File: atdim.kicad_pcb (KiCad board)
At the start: 2 copper layers, 49.8 x 24.9 mm, 17 parts, among them IC1 ATTINY85-T, P1 CONN_4, P2 ICSP, Q1 MOSFET_N, U1 7805

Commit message: switch to 47K sense resistor for better match for 5549 response
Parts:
- R1: value 10K -> 47K
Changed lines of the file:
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@@
       (effects (font (size 1.397 1.27) (thickness 0.2032)))
     )
-    (fp_text value 10K (at 0 0.127 180) (layer F.SilkS)
+    (fp_text value 47K (at 0 0.127 180) (layer F.SilkS)
       (effects (font (size 1.397 1.27) (thickness 0.2032)))
     )

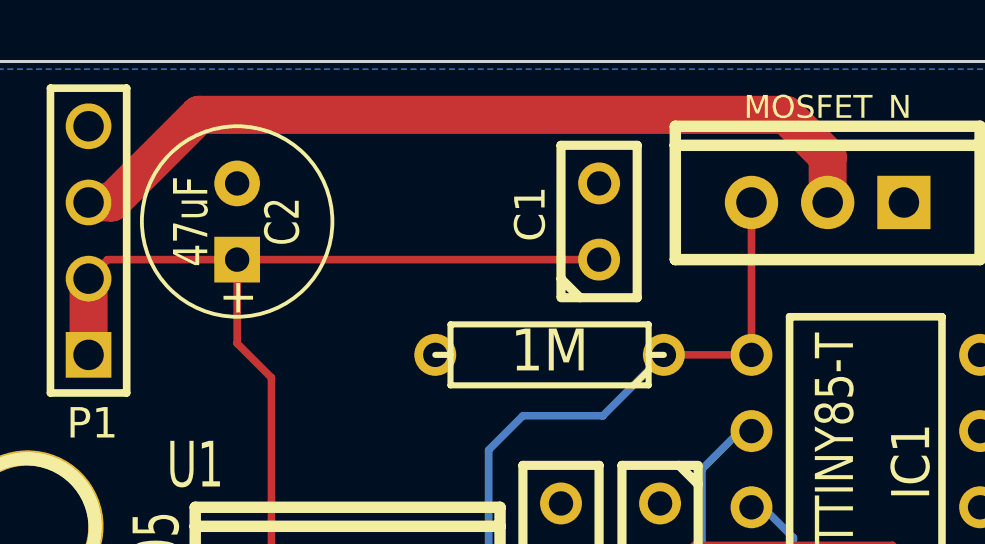
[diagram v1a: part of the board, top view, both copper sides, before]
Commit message: added pull-up resistor, changed some component values
Added pull-up resistor based on writeup at
https://gasstationwithoutpumps.wordpress.com/2014/07/28/pwm-controller/

Modified suggested capacitor values based on additional perusal of
data sheets for various versions of components.

Modified suggested R1 value based on experiments with my existing LDRs
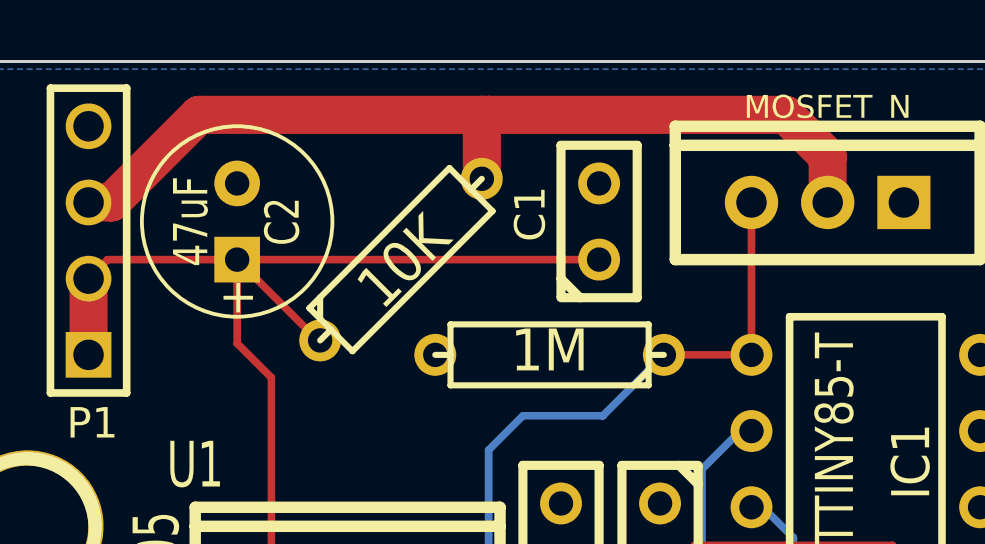
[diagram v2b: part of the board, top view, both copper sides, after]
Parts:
- added R3: 10K, R3, F.Cu at (116.3, 106.7)
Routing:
- net +12V: track 31.1 -> 35.0 mm
- net /DRAIN: track 28.0 -> 30.5 mm
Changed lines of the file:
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@@
 (kicad_pcb (version 3) (host pcbnew "(2013-june-11)-stable")
   (general
-    (links 33)
+    (links 35)
     (no_connects 0)
     (area 99.6315 100.025999 150.241 125.1966)
     (thickness 1.6)
     (drawings 4)
-    (tracks 79)
+    (tracks 86)
     (zones 0)
-    (modules 17)
+    (modules 18)
     (nets 11)
   )
@@
     )
   )
+  (module R3 (layer F.Cu)
+    (at 116.332 106.68 45)
+    (descr "Resitance 3 pas")
+    (tags R)
+    (autoplace_cost180 10)
+    (fp_text reference R3 (at 0 0.127 45) (layer F.SilkS) hide
+      (effects (font (size 1.397 1.27) (thickness 0.2032)))
+    )
+    (fp_text value 10K (at 0 0.127 45) (layer F.SilkS)
+      (effects (font (size 1.397 1.27) (thickness 0.2032)))
+    )
+    (fp_line (start -3.81 0) (end -3.302 0) (layer F.SilkS) (width 0.2032))
+    (fp_line (start 3.81 0) (end 3.302 0) (layer F.SilkS) (width 0.2032))
+    (fp_line (start 3.302 0) (end 3.302 -1.016) (layer F.SilkS) (width 0.2032))
+    (fp_line (start 3.302 -1.016) (end -3.302 -1.016) (layer F.SilkS) (width 0.2032))
+    (fp_line (start -3.302 -1.016) (end -3.302 1.016) (layer F.SilkS) (width 0.2032))
+    (fp_line (start -3.302 1.016) (end 3.302 1.016) (layer F.SilkS) (width 0.2032))
+    (fp_line (start 3.302 1.016) (end 3.302 0) (layer F.SilkS) (width 0.2032))
+    (fp_line (start -3.302 -0.508) (end -2.794 -1.016) (layer F.SilkS) (width 0.2032))
+    (pad 1 thru_hole circle (at -3.81 0 45) (size 1.397 1.397) (drill 0.8128)
+      (layers *.Cu *.Mask F.SilkS)
+      (net 1 +12V)
+    )
+    (pad 2 thru_hole circle (at 3.81 0 45) (size 1.397 1.397) (drill 0.8128)
+      (layers *.Cu *.Mask F.SilkS)
+      (net 4 /DRAIN)
+    )
+    (model discret/resistor.wrl
+      (at (xyz 0 0 0))
+      (scale (xyz 0.3 0.3 0.3))
+      (rotate (xyz 0 0 0))
+    )
+  )
   (gr_line (start 100.076 124.968) (end 100.076 100.076) (angle 90) (layer Edge.Cuts) (width 0.1))
   (gr_line (start 149.86 124.968) (end 100.076 124.968) (angle 90) (layer Edge.Cuts) (width 0.1))
   (gr_line (start 149.86 100.076) (end 149.86 124.968) (angle 90) (layer Edge.Cuts) (width 0.1))
   (gr_line (start 100.076 100.076) (end 149.86 100.076) (angle 90) (layer Edge.Cuts) (width 0.1))
+  (segment (start 113.637923 109.374077) (end 113.565077 109.374077) (width 0.254) (layer F.Cu) (net 1))
+  (segment (start 113.565077 109.374077) (end 110.871 106.68) (width 0.254) (layer F.Cu) (net 1))
   (segment (start 110.871 106.68) (end 110.871 109.474) (width 0.254) (layer F.Cu) (net 1))
   (segment (start 112.014 110.617) (end 112.014 117.475) (width 0.254) (layer F.Cu) (net 1))
@@
   (segment (start 137.16 115.697) (end 137.16 121.793) (width 0.254) (layer F.Cu) (net 3))
   (segment (start 136.398 114.935) (end 137.16 115.697) (width 0.254) (layer F.Cu) (net 3))
+  (segment (start 119.026077 103.985923) (end 119.026077 101.854) (width 1.27) (layer F.Cu) (net 4))
+  (segment (start 119.253 101.981) (end 119.253 101.854) (width 1.27) (layer F.Cu) (net 4))
+  (segment (start 119.153077 101.981) (end 119.253 101.981) (width 1.27) (layer F.Cu) (net 4))
+  (segment (start 119.026077 101.854) (end 119.153077 101.981) (width 1.27) (layer F.Cu) (net 4))
   (segment (start 105.918 104.775) (end 106.68 104.775) (width 1.27) (layer F.Cu) (net 4))
   (segment (start 130.556 103.251) (end 130.556 104.775) (width 1.27) (layer F.Cu) (net 4))
   (segment (start 129.159 101.854) (end 130.556 103.251) (width 1.27) (layer F.Cu) (net 4))
-  (segment (start 109.601 101.854) (end 129.159 101.854) (width 1.27) (layer F.Cu) (net 4))
+  (segment (start 109.601 101.854) (end 119.253 101.854) (width 1.27) (layer F.Cu) (net 4))
+  (segment (start 119.253 101.854) (end 129.159 101.854) (width 1.27) (layer F.Cu) (net 4))
   (segment (start 106.68 104.775) (end 109.601 101.854) (width 1.27) (layer F.Cu) (net 4))
   (segment (start 113.538 121.92) (end 114.935 123.317) (width 0.254) (layer B.Cu) (net 5))

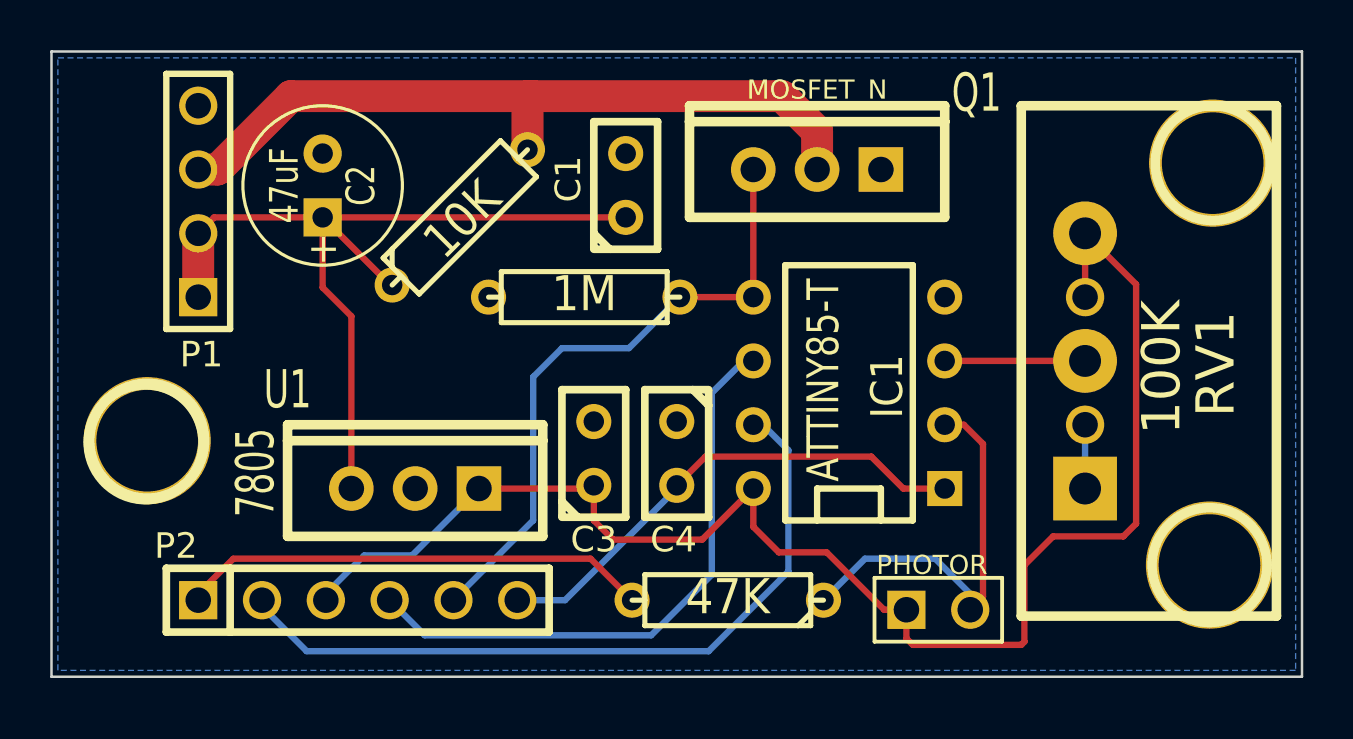
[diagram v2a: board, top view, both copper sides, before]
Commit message: add annotations on silkscreen for parts and connections
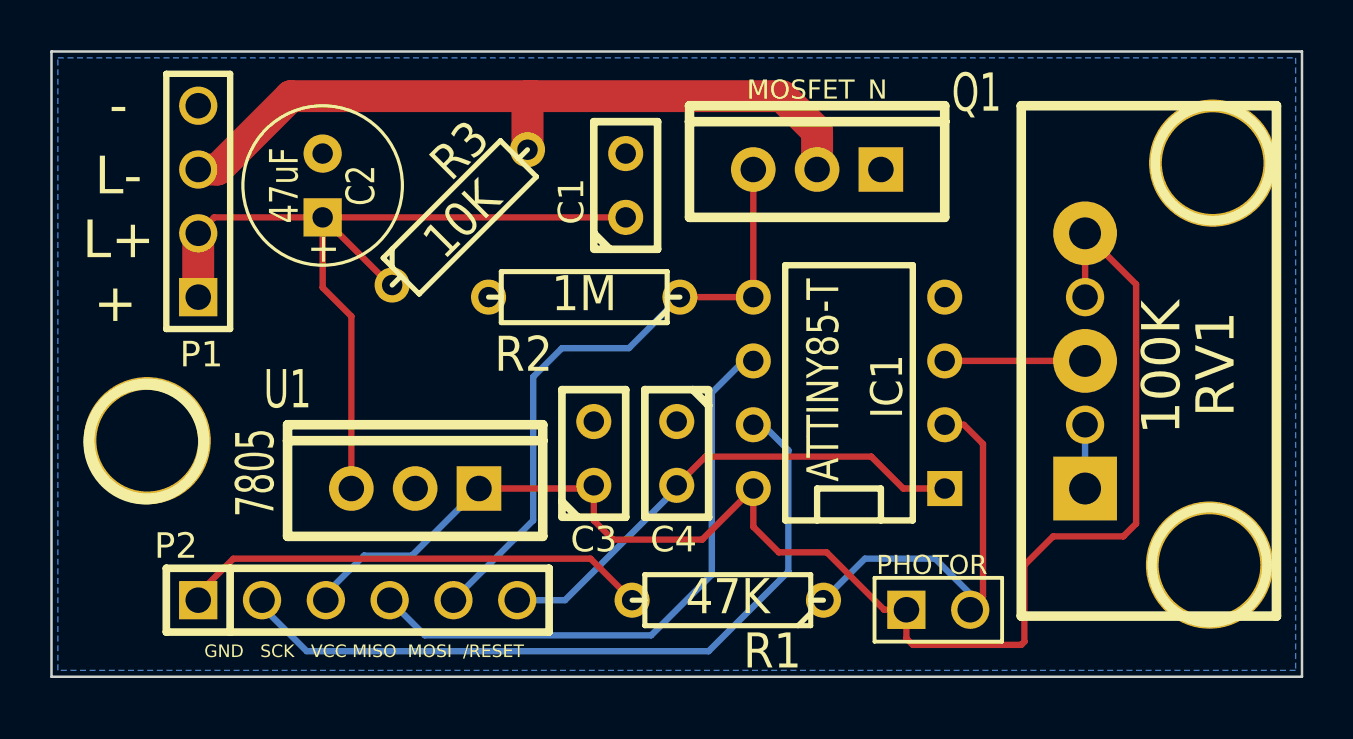
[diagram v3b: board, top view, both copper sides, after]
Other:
- board text added: "+"
- board text added: "-"
- board text added: "GND SCK VCC MISO MOSI /RESET"
- board text added: "L+"
- board text added: "L-"
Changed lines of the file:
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@@
     (links 35)
     (no_connects 0)
-    (area 99.6315 100.025999 150.241 125.1966)
+    (area 99.6315 100.025999 150.241 125.2601)
     (thickness 1.6)
-    (drawings 4)
+    (drawings 9)
     (tracks 86)
     (zones 0)
@@
     (tags R)
     (autoplace_cost180 10)
-    (fp_text reference R2 (at 0 0.127 180) (layer F.SilkS) hide
+    (fp_text reference R2 (at 2.413 -2.286 180) (layer F.SilkS)
       (effects (font (size 1.397 1.27) (thickness 0.2032)))
     )
@@
     (tags R)
     (autoplace_cost180 10)
-    (fp_text reference R1 (at 0 0.127 180) (layer F.SilkS) hide
+    (fp_text reference R1 (at -1.778 -2.032 180) (layer F.SilkS)
       (effects (font (size 1.397 1.27) (thickness 0.2032)))
     )
@@
     (descr "Condensateur e = 1 pas")
     (tags C)
-    (fp_text reference C1 (at 0.254 -2.286 90) (layer F.SilkS)
+    (fp_text reference C1 (at -0.635 -2.159 90) (layer F.SilkS)
       (effects (font (size 1.016 1.016) (thickness 0.2032)))
     )
@@
     (tags R)
     (autoplace_cost180 10)
-    (fp_text reference R3 (at 0 0.127 45) (layer F.SilkS) hide
+    (fp_text reference R3 (at 1.885854 -1.885854 45) (layer F.SilkS)
       (effects (font (size 1.397 1.27) (thickness 0.2032)))
     )
@@
     )
   )
+  (gr_text "GND   SCK   VCC MISO  MOSI  /RESET" (at 112.522 123.952) (layer F.SilkS)
+    (effects (font (size 0.5 0.5) (thickness 0.125)))
+  )
+  (gr_text L- (at 102.743 105.029) (layer F.SilkS)
+    (effects (font (size 1.5 1.5) (thickness 0.3)))
+  )
+  (gr_text L+ (at 102.743 107.569) (layer F.SilkS)
+    (effects (font (size 1.5 1.5) (thickness 0.3)))
+  )
+  (gr_text + (at 102.616 110.109) (layer F.SilkS)
+    (effects (font (size 1.5 1.5) (thickness 0.3)))
+  )
+  (gr_text - (at 102.743 102.235) (layer F.SilkS)
+    (effects (font (size 1.5 1.5) (thickness 0.3)))
+  )
   (gr_line (start 100.076 124.968) (end 100.076 100.076) (angle 90) (layer Edge.Cuts) (width 0.1))

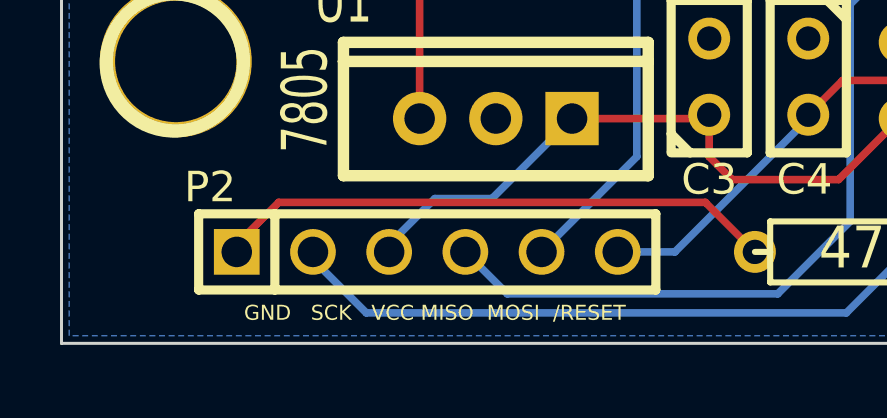
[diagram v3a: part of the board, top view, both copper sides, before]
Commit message: mark RESET pin with overbar
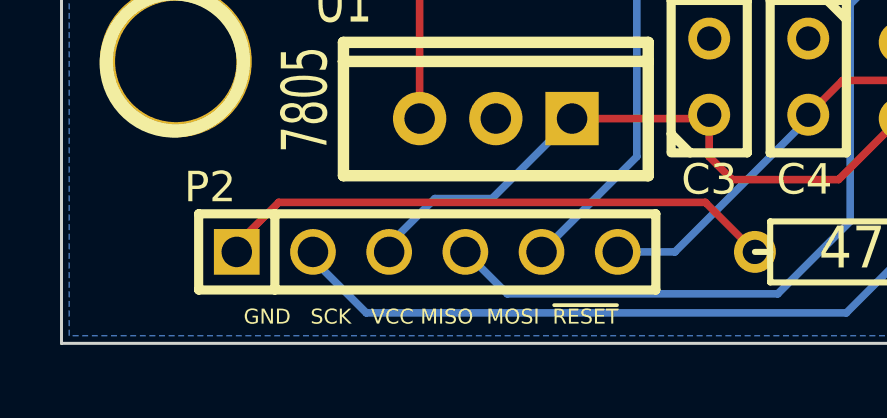
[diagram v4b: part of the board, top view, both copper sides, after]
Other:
- board text added: "GND SCK VCC MISO MOSI ~RESET"
- board text removed: "GND SCK VCC MISO MOSI /RESET"
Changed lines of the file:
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@@
     )
   )
-  (gr_text "GND   SCK   VCC MISO  MOSI  /RESET" (at 112.522 123.952) (layer F.SilkS)
+  (gr_text "GND   SCK   VCC MISO  MOSI  ~RESET" (at 112.395 124.079) (layer F.SilkS)
     (effects (font (size 0.5 0.5) (thickness 0.125)))
   )

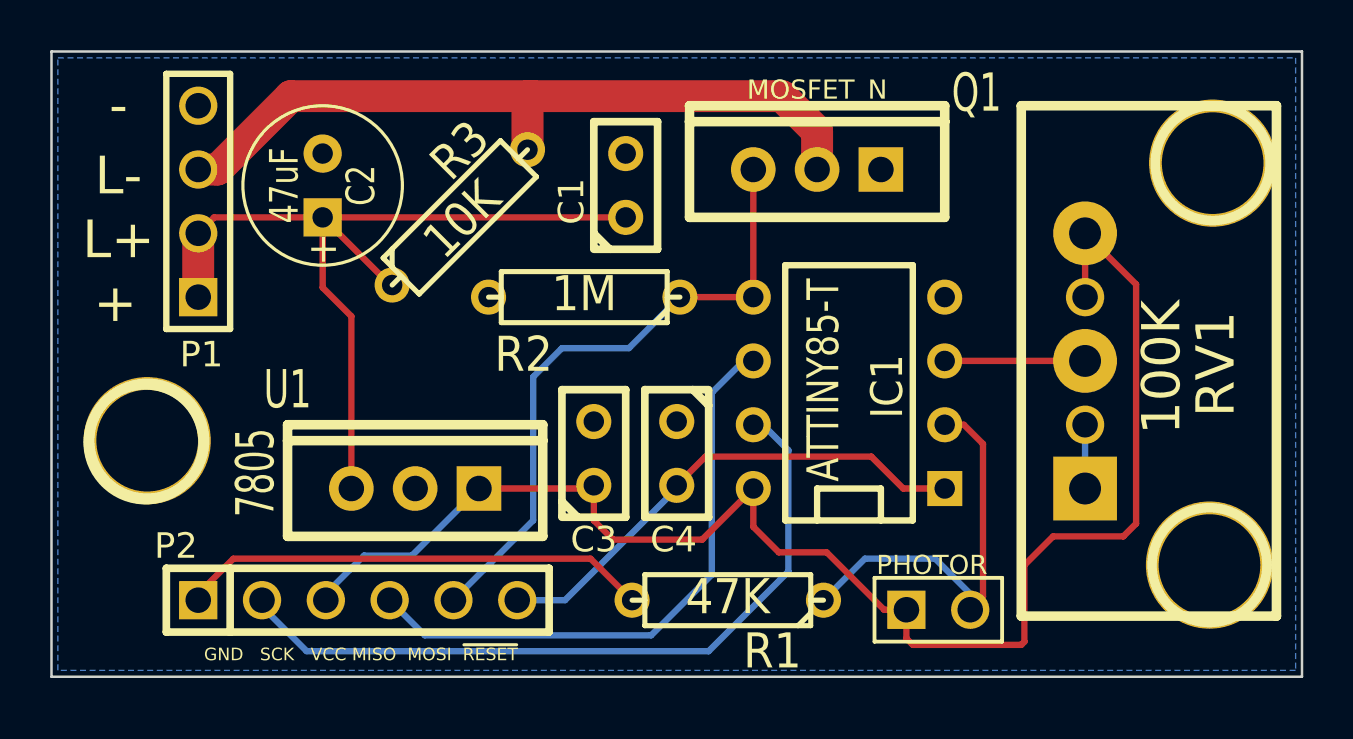
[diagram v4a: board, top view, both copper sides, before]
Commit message: rearrange board: separate power from logic, no need for reverse mounting or folding capacitor leads
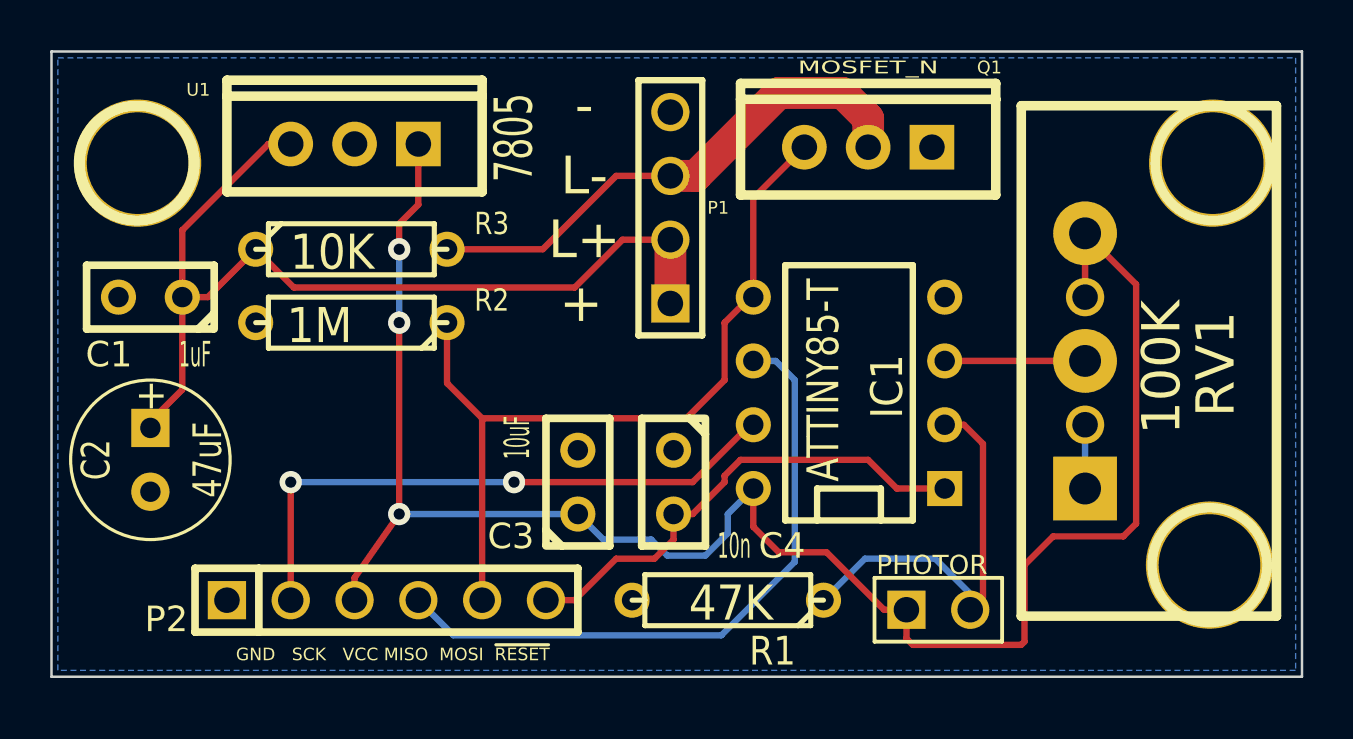
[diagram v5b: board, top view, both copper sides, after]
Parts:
- removed the 1PIN at (103.9, 115.6)
- removed the 1PIN at (103.8, 115.6)
- added 1PIN: P***, 1pin, F.Cu at (103.5, 104.5)
- added 1PIN: P***, 1pin, F.Cu at (103.4, 104.5)
- moved C1 19.4 mm to (104.0, 109.9), turned to 180 degrees
- moved P1 18.8 mm to (124.7, 106.3)
- moved U1 13.9 mm to (112.1, 103.8)
- moved C2 12.9 mm to (104.0, 116.3), turned to 270 degrees
- moved R2 9.33 mm to (112.0, 110.9)
- moved R3 4.50 mm to (112.0, 108.0), turned to 0 degrees
- moved Q1 2.22 mm to (132.6, 103.9)
- moved C3 1.31 mm to (121.0, 117.2)
- moved C4 1.15 mm to (124.8, 117.2)
- moved P2 1.14 mm to (113.4, 121.9)
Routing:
- net GND: track 21.3 -> 2.54 mm
- net /VCC: track 59.7 -> 73.5 mm, vias 0 -> 3
- net /DRAIN: track 30.5 -> 20.9 mm
- net /MOSI: track 25.4 -> 32.6 mm
- net +12V: track 35.0 -> 40.9 mm
- net /SCK: track 29.9 -> 24.1 mm, vias 0 -> 2
- net /MISO: track 23.8 -> 26.0 mm
- net /~RESET: track 20.0 -> 19.4 mm

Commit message: add a fusible resistor
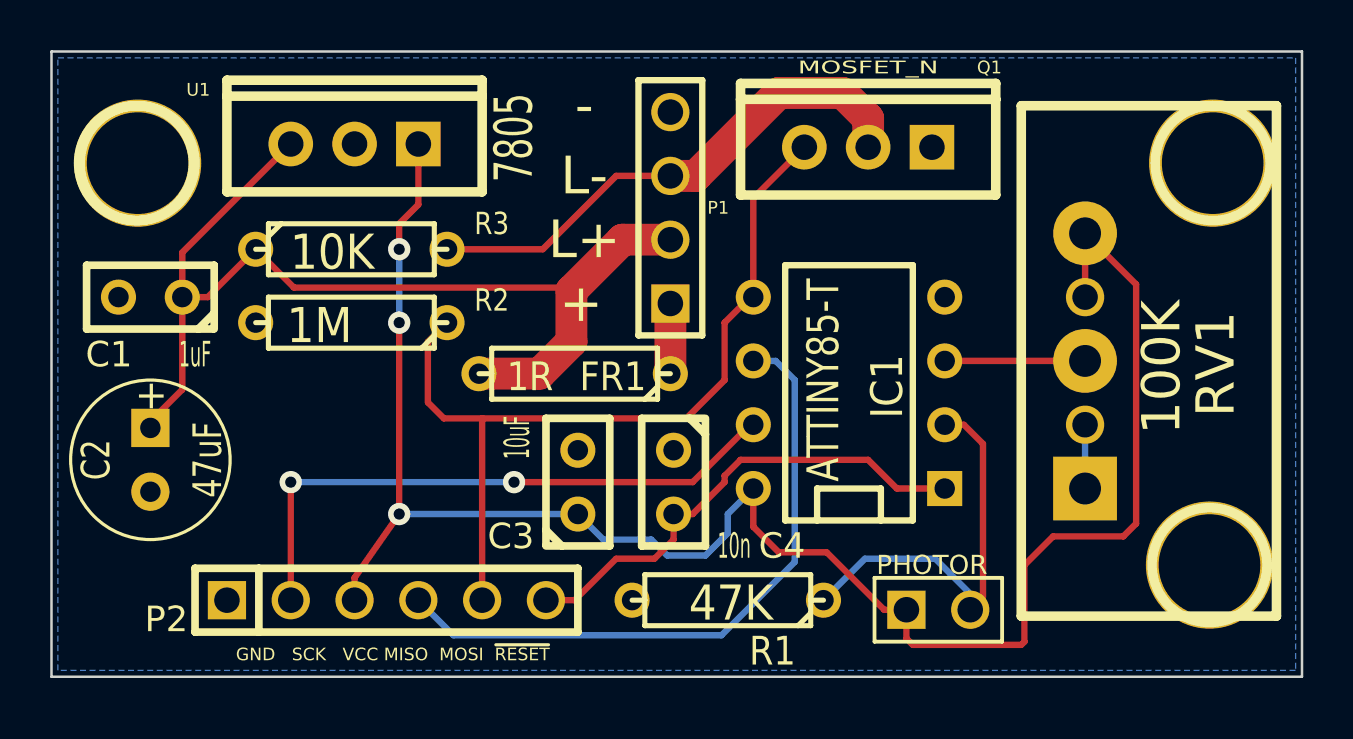
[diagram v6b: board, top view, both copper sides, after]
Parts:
- added FR1: 1R, R3, F.Cu at (120.9, 112.9)
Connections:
- C1 pad 1: +12V -> /+12VS
- C2 pad 1: +12V -> /+12VS
- P1 pad 2: +12V -> /+12VS
- R3 pad 1: +12V -> /+12VS
- U1 pad VI: +12V -> /+12VS
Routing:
- net /+12VS: track 0.00 -> 41.6 mm
- net +12V: track 40.9 -> 2.79 mm
- net /MOSI: track 32.6 -> 34.1 mm
